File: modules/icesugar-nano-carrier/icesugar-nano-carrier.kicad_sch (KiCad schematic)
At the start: 3 parts, among them J1 Conn_01x06_Pin, J2 Conn_01x06_Pin, J3 Conn_02x06_Odd_Even

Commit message: finish ICESugar Nano carrier board design
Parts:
- added M1: ~, MegaCastle:MegaCastle2x18-Module-I24.0x40.9-M800067FFF, symbol MegaCastle:MegaCastle2x18-Module-I24.0x40.9-M800067FFF
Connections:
- net +3.3V: now reaches J1.1 (Pin_1)
- net +3.3V: now also J2.6 (Pin_6), J3.11 (Pin_11), J3.12 (Pin_12), M1.1 (VCC)
- net GND: now reaches J1.2 (Pin_2)
- net GND: now also J2.5 (Pin_5), J3.10 (Pin_10), J3.9 (Pin_9), M1.18 (GND)
- net A1: now reaches J1.3 (Pin_3)
- net A1: now also M1.19
- net B1: now reaches J1.4 (Pin_4)
- net B1: now also M1.22
- net D1: now reaches J1.5 (Pin_5)
- net D1: now also M1.23
- net E2: now reaches J1.6 (Pin_6)
- net E2: now also M1.24
- net B4: now reaches J3.1 (Pin_1)
- net B4: now also M1.32
- net C6: now reaches J3.2 (Pin_2)
- net C6: now also M1.33
- net B5: now reaches J3.3 (Pin_3)
- net B5: now also M1.31
- net E3: now reaches J3.4 (Pin_4)
- net E3: now also M1.34
- net E1: now reaches J3.5 (Pin_5)
- net E1: now also M1.30
- net C2: now reaches J3.6 (Pin_6)
- net C2: now also M1.35
- net B1_DUP: now reaches J3.7 (Pin_7)
- net B1_DUP: now also M1.29
- net A1_DUP: now reaches J3.8 (Pin_8)
- net A1_DUP: now also M1.36
- net B3: now reaches J2.1 (Pin_1)
- net B3: now also M1.28
- net A3: now reaches J2.2 (Pin_2)
- net A3: now also M1.27
- net B6: now reaches J2.3 (Pin_3)
- net B6: now also M1.26
- net C5: now reaches J2.4 (Pin_4)
- net C5: now also M1.25
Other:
- note added: "Why on earth are A1 and B1 connected to two different PMODs, when there are unused pins on the FPGA?"
- moved on the sheet: J3

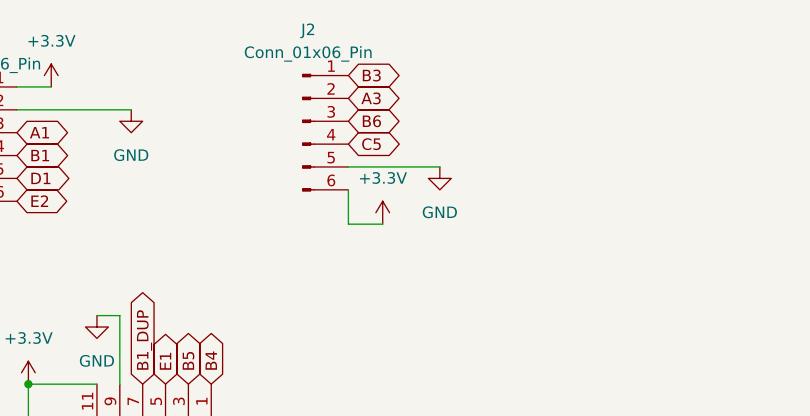
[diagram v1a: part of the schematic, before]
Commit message: fix icesugar nano carrier pinout
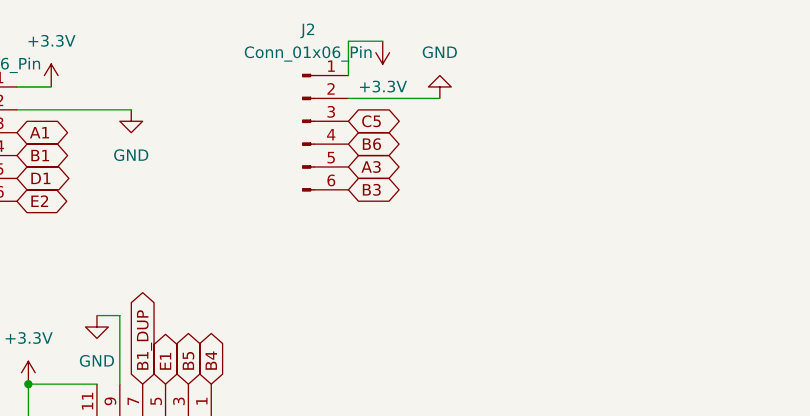
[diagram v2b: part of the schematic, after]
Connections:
- net +3.3V: now also J2.1 (Pin_1); no longer J2.6 (Pin_6)
- net A3: now also J2.5 (Pin_5); no longer J2.2 (Pin_2)
- net B3: now also J2.6 (Pin_6); no longer J2.1 (Pin_1)
- net B6: now also J2.4 (Pin_4); no longer J2.3 (Pin_3)
- net C5: now also J2.3 (Pin_3); no longer J2.4 (Pin_4)
- net GND: now also J2.2 (Pin_2); no longer J2.5 (Pin_5)
